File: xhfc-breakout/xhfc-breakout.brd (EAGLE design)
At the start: 109.2 x 50 mm, 78 parts, among them Q1 BC848CSMD, Q2 BC848CSMD, Q3 BC848CSMD, Q4 BC848CSMD, U1 XHFC-2SU, X1 UEXT

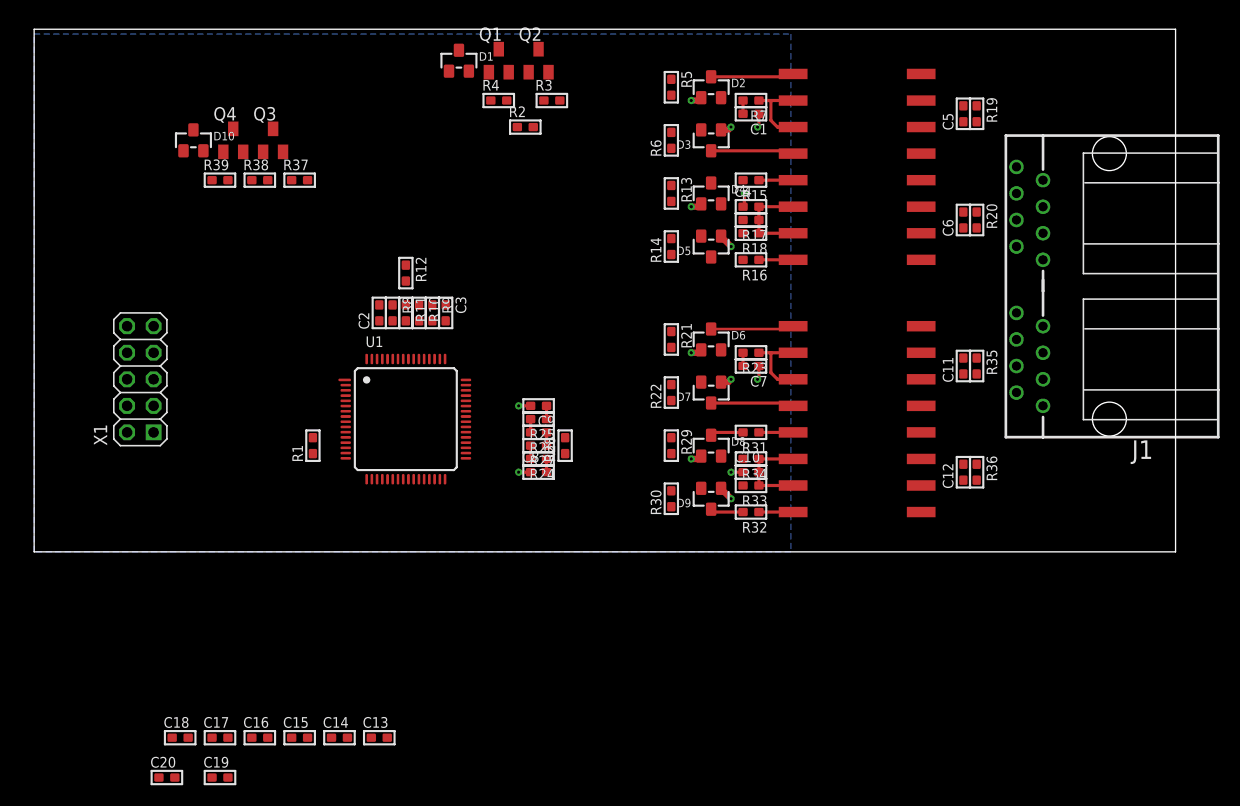
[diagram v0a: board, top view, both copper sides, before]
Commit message: xhfc-breakout: more WIP layout + schematics work
schematics should be done now, layout about 65%
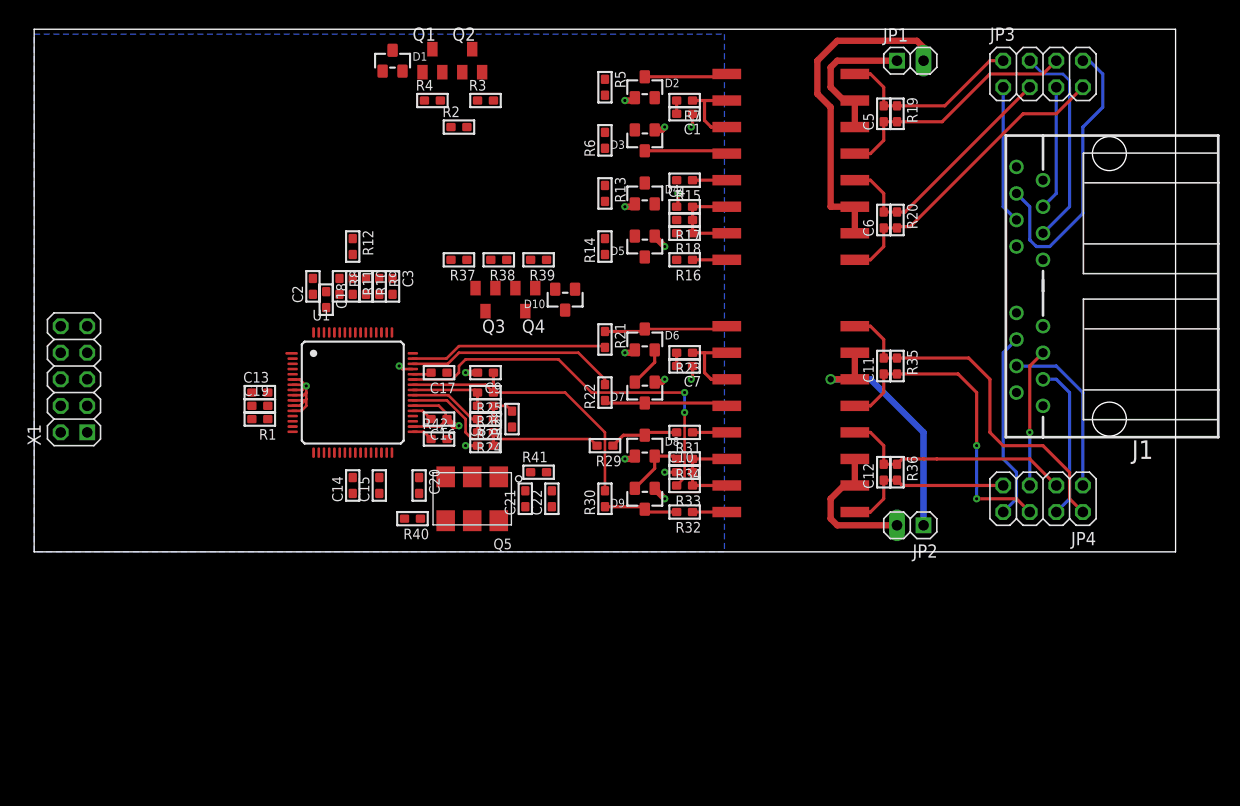
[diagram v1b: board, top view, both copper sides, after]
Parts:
- added C21, C22: 10n, rc-sysmocom:_0603
- added JP1, JP2: (no value), laforge:1X02
- added JP3, JP4: (no value), pinhead:2X04
- added Q5: (no value), tcxo:VKB
- added R40, R42: 47, rc-sysmocom:_0603
- added R41: 1k5, rc-sysmocom:_0603
- C20: value 33n -> 10n
- moved C18 44.2 mm to (27.9, 24.1), turned to 270 degrees
- moved C17 40.7 mm to (38.7, 17.1), turned to 180 degrees
- moved D10 38.7 mm to (50.8, 24.1), turned to 180 degrees
- moved C20 36.9 mm to (36.8, 6.35), turned to 270 degrees
- moved C19 35.8 mm to (21.6, 14.0)
- moved C16 35.0 mm to (38.7, 12.7), turned to 180 degrees
- moved C13 34.9 mm to (21.6, 15.2)
- moved Q4 31.8 mm to (47.0, 24.1), turned to 180 degrees
- moved R39 31.4 mm to (48.3, 27.9), turned to 180 degrees
- moved Q3 25.4 mm to (43.2, 24.1), turned to 180 degrees
- moved C15 25.3 mm to (33.0, 6.35), turned to 90 degrees
- moved C14 24.2 mm to (30.5, 6.35), turned to 90 degrees
- moved R38 24.1 mm to (44.5, 27.9), turned to 180 degrees
- moved R37 17.0 mm to (40.6, 27.9), turned to 180 degrees
- moved C11 7.62 mm to (81.3, 17.8)
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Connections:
- new net CLK_OUT: R42.2
- new net N$50: C6.2, JP3.3, R20.1, TR1.P$4
- new net N$52: J1.2-3, JP3.4
- new net N$53: J1.2-6, JP3.8
- new net N$54: J1.1-4, JP4.1
- new net N$55: J1.1-5, JP4.5
- new net N$56: J1.1-3, JP4.4
- new net N$61: J1.1-6, JP4.8
- new net N$62: C21.2, Q5.1, R41.1
- new net N$63: R42.1, U1.33
- new net N$64: Q5.4, R40.1
- new net N$8: J1.2-4, JP3.1
- new net VCXO_OUT: R40.2, U1.30
- new net VCXO_VCTRL: C22.2, R41.2
- net !INT: now also X1.4
- net !RES: now also X1.3
- net GND: now also C21.1, C22.1, Q5.3, U1.34
- net N$18: now also JP3.2; no longer J1.2-5
- net N$21: now also JP3.6; no longer J1.2-4
- net N$25: now also J1.2-5, JP3.5; no longer C6.2, J1.2-6, R20.1, TR1.P$4
- net N$26: now also JP3.7; no longer J1.2-3
- net N$43: now also JP4.2; no longer J1.1-4
- net N$44: now also JP4.6; no longer J1.1-5
- net N$45: now also JP4.3; no longer J1.1-3
- net N$46: now also JP4.7; no longer J1.1-6
- net NTPWR0+: now also JP1.2
- net NTPWR0-: now also JP1.1
- net NTPWR1+: now also JP2.2
- net NTPWR1-: now also JP2.1
- net VCC: now also Q5.2, Q5.5, Q5.6
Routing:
- net N$32: track 0.00 -> 37.7 mm, vias 0 -> 2
- net N$43: track 0.00 -> 34.7 mm
- net NTPWR0+: track 0.00 -> 31.8 mm
- net N$44: track 0.00 -> 30.5 mm, vias 0 -> 2
- net N$26: track 0.00 -> 29.7 mm
- net N$53: track 0.00 -> 28.2 mm
- net N$33: track 1.27 -> 27.8 mm
- net NTPWR1-: track 0.00 -> 25.0 mm, vias 0 -> 1
- net N$21: track 0.00 -> 24.0 mm
- net N$50: track 0.00 -> 24.0 mm
- net N$45: track 0.00 -> 22.8 mm
- net GND: track 16.6 -> 39.0 mm, vias 14 -> 17
- net N$34: track 1.27 -> 21.7 mm
- net N$29: track 0.00 -> 20.4 mm
- net N$52: track 0.00 -> 20.3 mm
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
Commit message: xhfc-breakout: Complete routing of v1 board
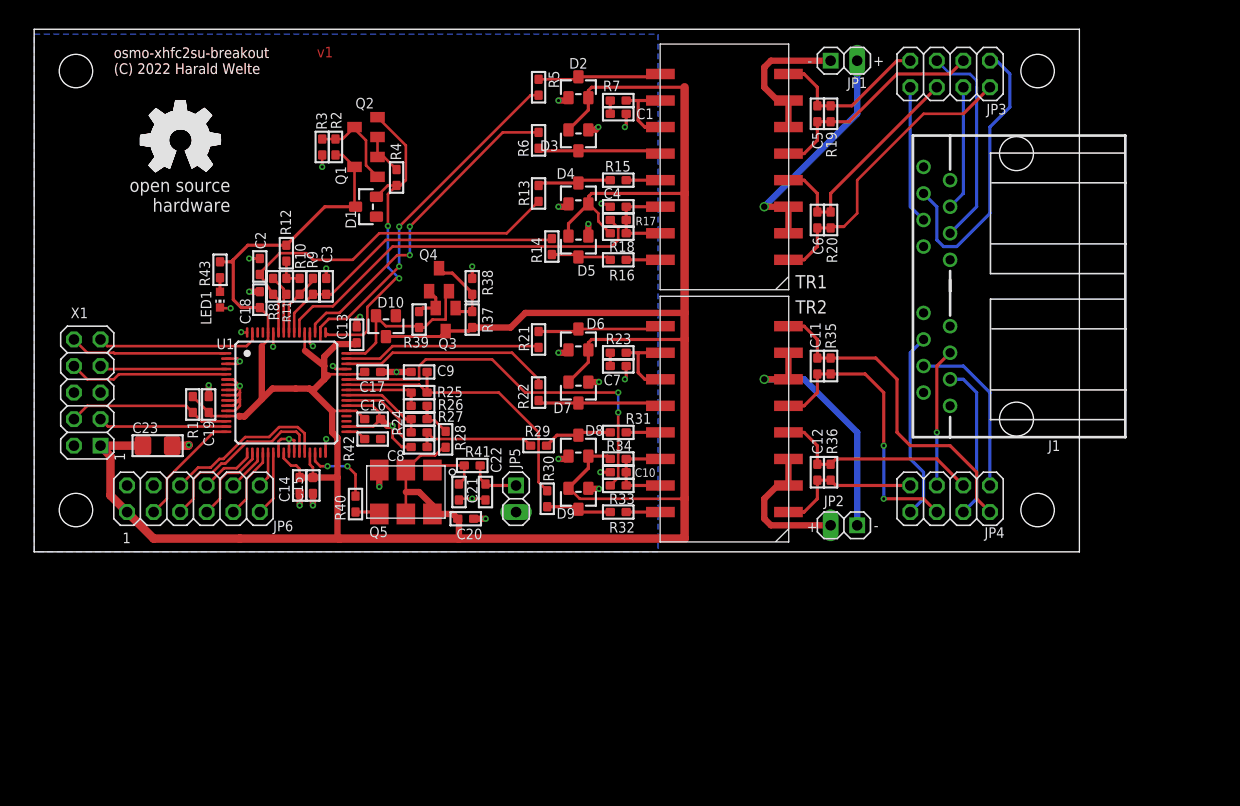
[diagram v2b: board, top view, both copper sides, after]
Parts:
- added C23: 10u, rc-sysmocom:1206
- added JP5: (no value), laforge:1X02
- added JP6: (no value), pinhead:2X06
- added LED1: green, led:CHIP-LED0603
- added R43: 330, rc-sysmocom:_0603
- added U$1: (no value), oshw:OSHW_8MM_COPPER
- added U$2: (no value), oshw:OSHW_8MM
- moved D10 17.3 mm to (33.7, 21.6)
- moved R3 16.2 mm to (27.6, 38.7), turned to 90 degrees
- moved D1 14.2 mm to (31.8, 33.0), turned to 90 degrees
- moved R39 12.8 mm to (36.8, 22.2), turned to 90 degrees
- moved Q1 12.0 mm to (31.8, 36.8), turned to 90 degrees
- moved Q2 12.0 mm to (31.8, 40.6), turned to 90 degrees
- moved R2 12.0 mm to (28.8, 38.7), turned to 90 degrees
- moved C13 10.8 mm to (30.9, 20.8), turned to 270 degrees
- moved J1 8.89 mm to (94.0, 25.4)
- moved JP3 8.89 mm to (87.6, 45.7)
- moved JP4 8.89 mm to (87.6, 5.08)
- moved Q4 8.47 mm to (38.7, 26.0), turned to 0 degrees
- moved R4 8.13 mm to (34.7, 35.8), turned to 90 degrees
- moved R28 6.64 mm to (39.4, 10.8)
- moved R1 6.56 mm to (15.2, 14.1), turned to 90 degrees
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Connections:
- net N$11 renamed P0_R_B
- net N$12 renamed P0_R_A
- net N$13 renamed P0_L_A
- net N$14 renamed P0_ADJ
- net N$15 renamed P0_L_B
- net N$2 renamed P0_T_B
- net N$28 renamed P1_T_B
- net N$29 renamed P1_T_A
- net N$32 renamed P1_ADJ
- net N$33 renamed P1_R_B
- net N$34 renamed P1_R_A
- net N$35 renamed P1_L_A
- net N$36 renamed P1_L_B
- net N$4 renamed P0_VDD_SU
- net N$49 renamed P1_VDD_SU
- net N$5 renamed P0_T_A
- removed net N$51: U1.27
- removed net N$57: U1.17
- removed net N$58: U1.16
- new net F1_1: JP6.5, U1.27
- new net N$2: LED1.A, R43.1
- new net SYNC_I: JP6.8, U1.17
- new net SYNC_O: JP6.3, U1.16
- net GND: now also C23.2, JP5.2, JP6.2, LED1.C
- net PCM_2M_CLK: now also JP6.7
- net PCM_4M_CLK: now also JP6.10
- net PCM_ALT_FRAME: now also JP6.6
- net PCM_DATA_IO: now also JP6.11
- net PCM_DATA_OI: now also JP6.12
- net PCM_FRAME: now also JP6.9
- net VCC: now also C23.1, JP6.1, R43.2, X1.1
- net VCXO_VCTRL: now also JP5.1
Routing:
- net VCC: track 13.8 -> 330.5 mm
- net P0_ADJ: track 0.00 -> 37.1 mm
- net P0_R_A: track 0.00 -> 36.3 mm
- net GND: track 39.0 -> 72.6 mm, vias 17 -> 36
- net P0_T_B: track 0.00 -> 33.5 mm, vias 0 -> 2
- net P0_T_A: track 0.00 -> 31.4 mm, vias 0 -> 2
- net P0_VDD_SU: track 0.00 -> 31.0 mm, vias 0 -> 2
- net P0_R_B: track 0.00 -> 29.5 mm
- net F1_1: track 0.00 -> 17.6 mm
- net PCM_ALT_FRAME: track 0.00 -> 16.3 mm
- net P1_VDD_SU: track 0.00 -> 16.1 mm
- net SPI_CLK: track 0.00 -> 15.8 mm
- net !INT: track 0.00 -> 15.7 mm
- net SPI_MOSI: track 0.00 -> 15.3 mm
- net !SPI_SEL: track 0.00 -> 15.0 mm
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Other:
- board size 109.2 x 50 mm -> 100 x 50 mm
- board text added: "+"
- board text added: "-"
- board text added: "1"
- board text added: ">VERSION"
- board text added: "osmo-xhfc2su-breakout (C) 2022 Harald Welte"

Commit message: xhfc-breakout: Fix some part values; documentation
* R18 + R34 are 330k and not 3k9
* R5, R6, R21, R22 are 3R3 instead of 62R in universal TE/NT
* add various documentation text snippets
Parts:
- R18, R34: value 3k9 -> 330k
- R21: value 62 -> 62 (3R3 universaal)
- R22, R5, R6: value 62 -> 62 (3R3 universal)

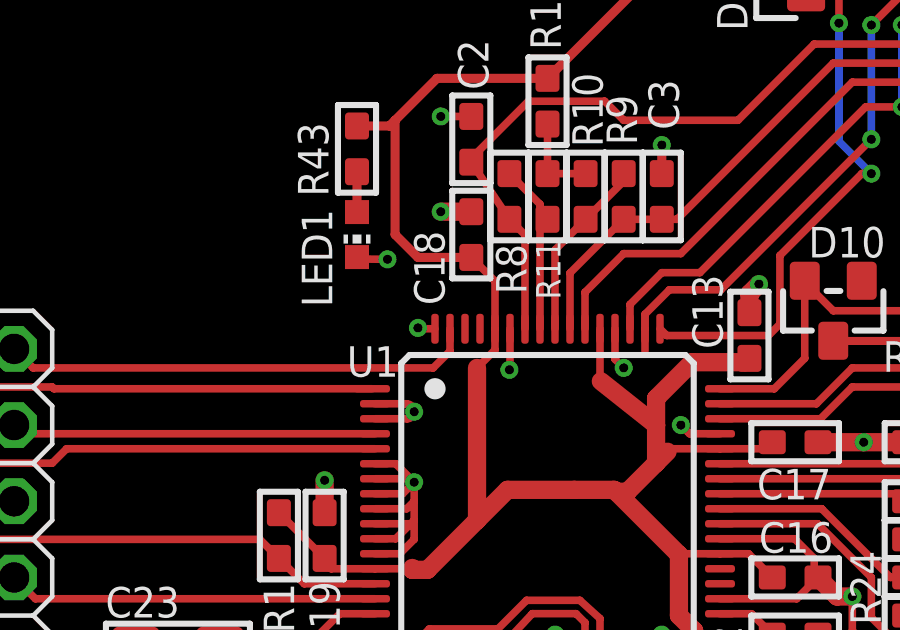
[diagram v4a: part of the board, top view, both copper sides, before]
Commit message: xhfc-breaout: Conncet SPI_INV to GND
This was missing from the v1 design. SPI_INV must be tied to either high
or low to select the SPI clock polarity.  It was tied to low by manawyrm
in his manual rework, so let's reflect this in the design accordingly.
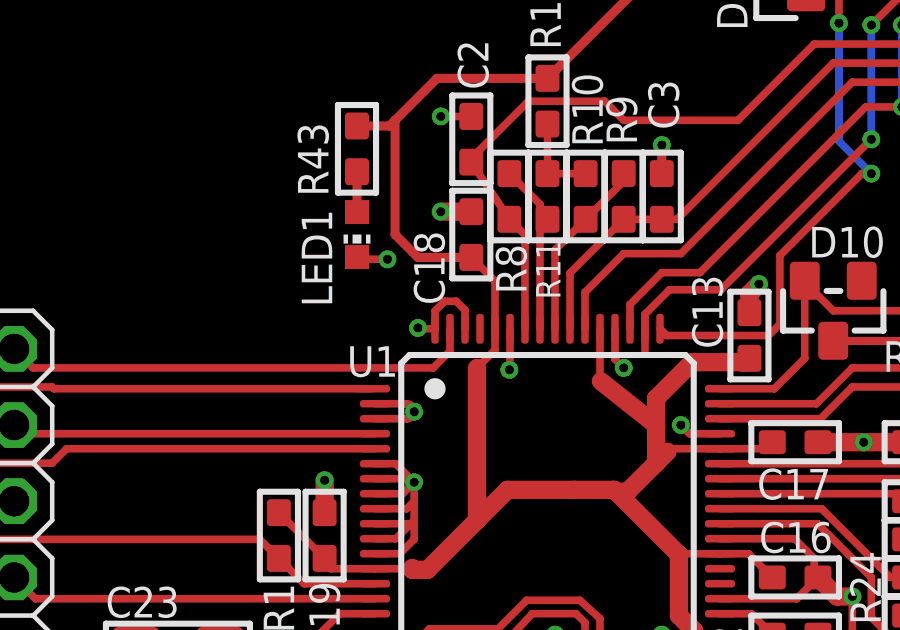
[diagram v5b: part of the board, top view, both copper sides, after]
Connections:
- removed net SPI_INV: U1.62
- net GND: now also U1.62
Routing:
- net GND: track 72.6 -> 75.0 mm
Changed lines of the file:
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@@
 <wire x1="35.179" y1="10.033" x2="34.29" y2="10.922" width="0.254" layer="1"/>
 <wire x1="34.29" y1="10.922" x2="34.29" y2="12.065" width="0.254" layer="1"/>
+<contactref element="U1" pad="62"/>
+<wire x1="21.38" y1="20.99" x2="21.38" y2="21.6095" width="0.254" layer="1"/>
+<wire x1="21.38" y1="21.6095" x2="21.082" y2="21.9075" width="0.254" layer="1"/>
+<wire x1="21.082" y1="21.9075" x2="20.701" y2="21.9075" width="0.254" layer="1"/>
+<wire x1="20.701" y1="21.9075" x2="20.3835" y2="21.59" width="0.254" layer="1"/>
+<wire x1="20.3835" y1="21.59" x2="20.3835" y2="20.9935" width="0.254" layer="1"/>
+<wire x1="20.3835" y1="20.9935" x2="20.38" y2="20.99" width="0.254" layer="1"/>
 </signal>
 <signal name="SPI_CLK">
@@
 <wire x1="6.985" y1="19.685" x2="20.32" y2="19.685" width="0.254" layer="1"/>
 </signal>
-<signal name="SPI_INV">
-<contactref element="U1" pad="62"/>
-</signal>
 <signal name="!RES">
